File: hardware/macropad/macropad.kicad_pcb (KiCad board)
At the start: 2 copper layers, 6.5 x 0.7 mm, 84 parts, among them J1 SWD, J2 USB_C_Receptacle, J3 Conn_01x04_Pin, J4 display(4x1), J5 USB_A, J6 Enc2, J6 enc2, J7 Conn_01x04_Pin, J7 Enc1, J8 USB_A, J9 Conn_02x03_Counter_Clockwise, Q1 Q_PMOS, Q2 FS8205A, SW1 SW_Push, SW10 SW_SPDT, SW11 SW_Push, SW12 Enc1, SW12 SW_Push, SW2 SW_Push, SW3 SW_Push, SW4 SW_Push, SW5 SW_Push, SW6 SW_Push, SW7 SW_Push, SW8 SW_Push, SW9 SW_Push, U1 AP2112K-3.3, U1 LP2992IM5-3.3/NOPB, U2 STM32F103C8Tx, U3 NRF24L01_Breakout, U4 STM32F103C8Tx, U5 NRF24L01_Breakout, U6 TP4056-42-ESOP8, U7 DW01A, U8 RT8010AGQW, Y1 8Mhz C_L=12pF, Y2 8Mhz

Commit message: added usba fp, updated pcb, 5v to vbus
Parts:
- removed C32: 0.1u, Capacitor_SMD:C_0603_1608Metric
- removed C33, C35: 10u, Capacitor_SMD:C_0805_2012Metric
- removed C34: 4.7u, Capacitor_SMD:C_0603_1608Metric
- removed J2: USB_C_Receptacle, usbc:TYPE-C-SMD_U263-163N-4GS1735
- removed the J6 at (85.9, 37.6)
- removed the J6 at (247.3, 72.9)
- removed the J7 at (42.6, 54.4)
- removed the J7 at (251.9, 72.9)
- removed J9: Conn_02x03_Counter_Clockwise, Connector_PinHeader_2.54mm:PinHeader_2x03_P2.54mm_Vertical
- removed Q1: Q_PMOS, Package_TO_SOT_SMD:SOT-23-3
- removed the R11 at (256.4, 72.1)
- removed the R11 at (34.3, 69.7)
- removed the R12 at (34.3, 72.7)
- removed the R12 at (256.4, 75.0)
- removed the SW12 at (74.9, 114.3)
- removed the SW12 at (26.8, 71.1)
- removed the U1 at (162.6, 130.5)
- removed the U1 at (268.1, 73.2)
- added C16: 10n, Capacitor_SMD:C_0603_1608Metric, F.Cu at (53.4, 163.9)
- added C24: 0.1u, Capacitor_SMD:C_0603_1608Metric, F.Cu at (75.8, 88.3)
- added C25: 0.1u, Capacitor_SMD:C_0603_1608Metric, F.Cu at (75.8, 90.8)
- added C26: 10u, Capacitor_SMD:C_0805_2012Metric, F.Cu at (76.0, 105.7)
- added C27: 4.7u, Capacitor_SMD:C_0603_1608Metric, F.Cu at (75.8, 93.3)
- added C28: 1u, Capacitor_SMD:C_0805_2012Metric, F.Cu at (76.0, 108.7)
- added C29: 10n, Capacitor_SMD:C_0603_1608Metric, F.Cu at (75.8, 95.9)
- added C30: 2.2u, Capacitor_SMD:C_0603_1608Metric, F.Cu at (75.8, 98.4)
- added J6: Enc2, Connector_PinHeader_2.54mm:PinHeader_1x05_P2.54mm_Vertical, F.Cu at (187.7, 97.8)
- added J7: Enc1, Connector_PinHeader_2.54mm:PinHeader_1x05_P2.54mm_Vertical, F.Cu at (187.7, 119.4)
- added R11: 10k, Resistor_SMD:R_0805_2012Metric, F.Cu at (89.3, 47.0)
- added R12: 10k, Resistor_SMD:R_0805_2012Metric, F.Cu at (112.6, 38.9)
- added SW12: SW_SPDT, Button_Switch_THT:SW_Slide_SPDT_Angled_CK_OS102011MA1Q, F.Cu at (65.5, 90.3)
- added SW13: SW_SPDT, Button_Switch_THT:SW_Slide_SPDT_Angled_CK_OS102011MA1Q, F.Cu at (65.5, 100.7)
- added U1: LP2992IM5-3.3/NOPB, LP2992:DBV0005A_N, F.Cu at (55.1, 180.6)
- added U9: LP2992IM5-3.3/NOPB, LP2992:DBV0005A_N, F.Cu at (63.9, 110.3)
- C21: footprint Capacitor_SMD:C_0805_2012Metric -> Capacitor_SMD:C_0603_1608Metric
- C31: value 0.1u -> 10u; footprint Capacitor_SMD:C_0603_1608Metric -> Capacitor_SMD:C_0805_2012Metric
- J3: moved to B.Cu
- J5: footprint Connector_PinHeader_2.54mm:PinHeader_1x05_P2.54mm_Horizontal -> usbA:U-G-O4DD-W-1
- J8: value USB_A -> Conn_01x02; footprint Connector_USB:USB_A_Connfly_DS1095 -> Connector_Wire:SolderWire-0.5sqmm_1x02_P4.6mm_D0.9mm_OD2.1mm
- R10: value 100 -> 1.2k
- R13: value 10k -> 1k; footprint Resistor_SMD:R_0805_2012Metric -> Resistor_SMD:R_0603_1608Metric
- R14: value 1.5K -> 100
- R6: value 1k -> 1.5K
- R7: value 1k -> 10k; footprint Resistor_SMD:R_0603_1608Metric -> Resistor_SMD:R_0805_2012Metric
- R8: value 1.2k -> 1k
- SW10: value SW_SPDT -> SW_Push; footprint keyswitches:Kailh_socket_MX -> Button_Switch_SMD:SW_Push_1P1T_NO_E-Switch_TL3301NxxxxxG; moved to B.Cu
- U8: footprint RT8010:WQFN16_RT8010_RIT-M -> RT8010:WQFN16_RT8010_RIT
- moved R3 244.8 mm to (41.2, 175.9)
- moved R13 184.3 mm to (79.8, 95.9)
- moved Q2 176.3 mm to (78.9, 101.9)
- moved D2 173.7 mm to (82.3, 113.1)
- moved U8 173.4 mm to (89.3, 112.9)
- moved U5 117.6 mm to (69.1, 158.1), turned to 90 degrees
- moved C13 113.3 mm to (36.7, 178.9)
- moved U4 109.7 mm to (74.5, 167.2), turned to -90 degrees
- moved SW10 100.4 mm to (74.2, 143.7), turned to 180 degrees
- moved C14 93.3 mm to (53.4, 158.9)
- moved C15 92.8 mm to (53.4, 161.4)
- moved U6 90.6 mm to (82.4, 107.6)
- moved J5 89.5 mm to (74.5, 177.8)
- moved Y1 87.3 mm to (142.7, 67.2)
- moved C21 85.2 mm to (57.4, 156.4)
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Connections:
- net /Power/out+ renamed out+
- C17 pad 2: GND_DGL -> GND
- C18 pad 2: GND_DGL -> GND
- C31 pad 1: +5V -> /Power/Vout_buck
- D1 pad 2: +5V -> VBUS
- D2 pad 2: +5V -> VBUS
- D3 pad 2: +5V -> VBUS
- J8 pad 1: VBUS -> /Power/B+
- J8 pad 2: /dongle/USB_D- -> /Power/B-
- L1 pad 2: /Power/Vout -> /Power/Vout_buck
- Q2 pad 6: GND -> /Power/out-
- Q2 pad 7: GND -> /Power/out-
- R10 pad 1: Net-(U7-VCC) -> Net-(U6-PROG)
- R10 pad 2: /Power/B+ -> GND
- R13 pad 1: /dongle/BOOT0_DGL -> Net-(U7-CS)
- R13 pad 2: GND_DGL -> /Power/out-
- R14 pad 1: +3.3V_DGL -> Net-(U7-VCC)
- R14 pad 2: /dongle/USB_D+_DGL -> /Power/B+
- R5 pad 1: +5V -> /dongle/BOOT0_DGL
- R5 pad 2: GND -> GND_DGL
- R6 pad 1: Net-(U6-~{CHRG}) -> +3.3V_DGL
- R6 pad 2: Net-(D1-K) -> /dongle/USB_D+_DGL
- R7 pad 1: Net-(U6-~{STDBY}) -> VBUS
- R7 pad 2: Net-(D3-K) -> GND
- R8 pad 1: Net-(U6-PROG) -> Net-(U6-~{CHRG})
- R8 pad 2: GND -> Net-(D1-K)
- R9 pad 1: Net-(U7-CS) -> Net-(U6-~{STDBY})
- R9 pad 2: GND -> Net-(D3-K)
- SW10 pad 1: /BAT_OUT_ON -> /dongle/NRST_DGL
- SW10 pad 2: /BAT_OUT -> GND_DGL
- U6 pad 4: +5V -> VBUS
- U6 pad 8: +5V -> VBUS
- U8 pad 4: /Power/Vout -> /Power/Vout_buck
- Y1 pad 2: GND_DGL -> GND
- Y1 pad 4: GND_DGL -> GND
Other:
- board outline removed

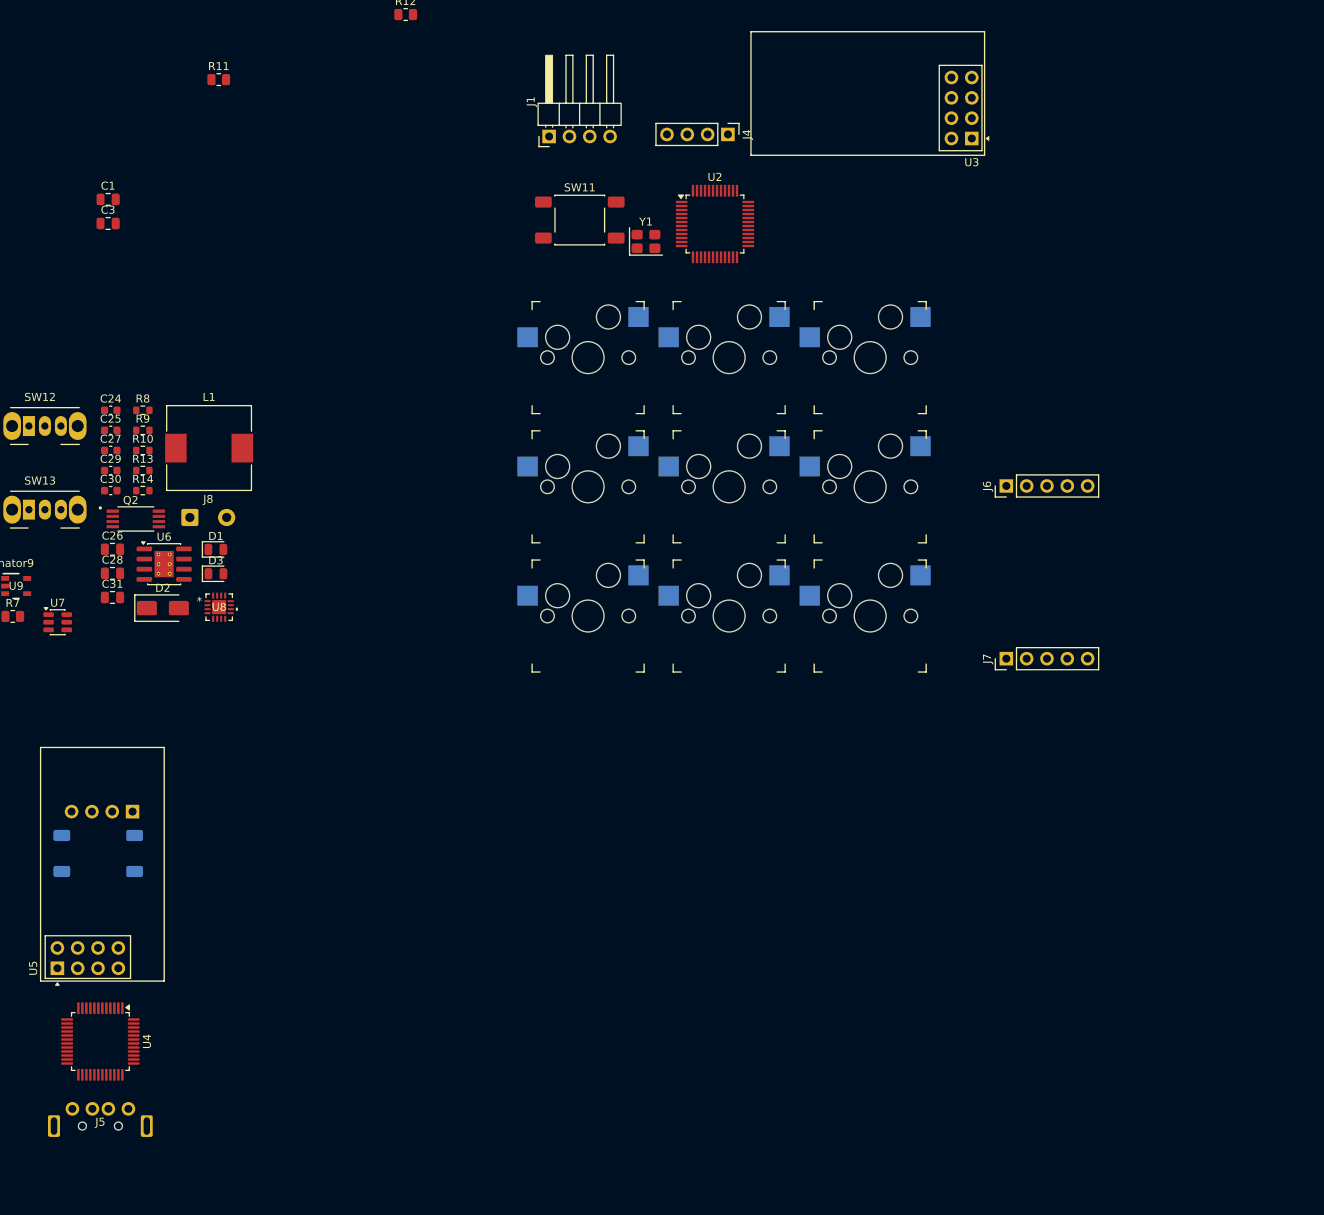
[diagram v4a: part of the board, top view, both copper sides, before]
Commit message: replaced buttons with pads
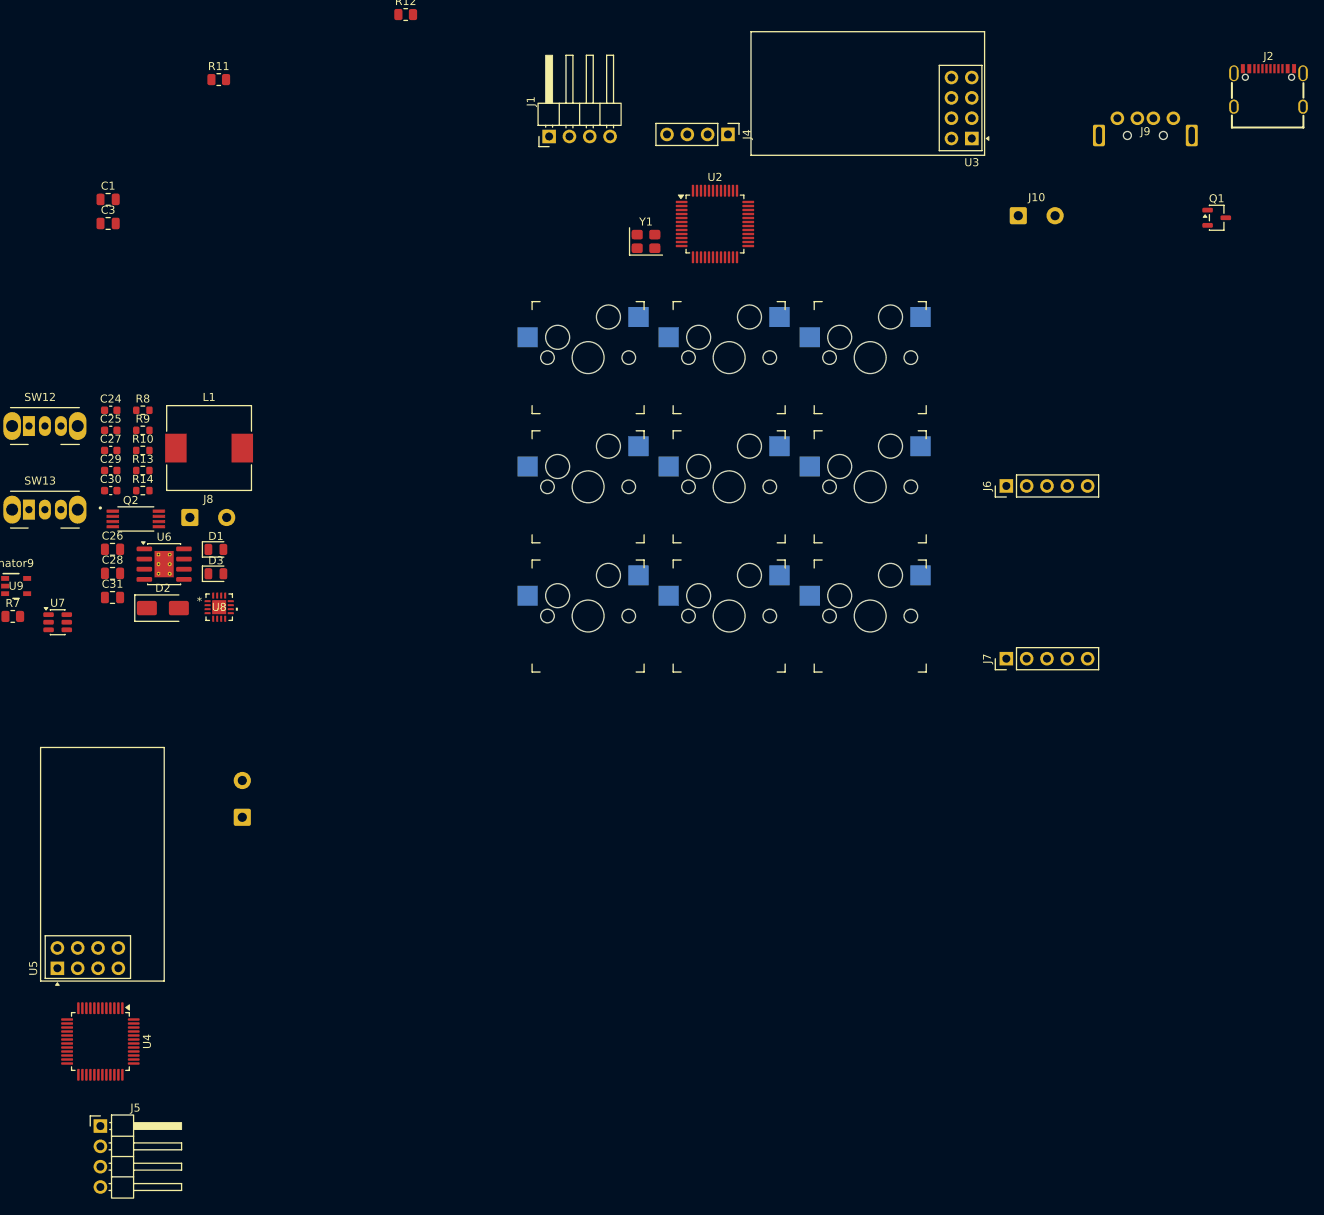
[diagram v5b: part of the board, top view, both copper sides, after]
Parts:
- removed SW10, SW11: SW_Push, Button_Switch_SMD:SW_Push_1P1T_NO_E-Switch_TL3301NxxxxxG
- added J10: Conn_01x02, Connector_Wire:SolderWire-0.5sqmm_1x02_P4.6mm_D0.9mm_OD2.1mm, F.Cu at (189.2, 64.0)
- added J2: USB_C_Receptacle, usbc:TYPE-C-SMD_U263-163N-4GS1735, F.Cu at (220.5, 48.0)
- added J9: USB_A, usbA:U-G-O4DD-W-1, F.Cu at (205.1, 54.0)
- added Q1: Q_PMOS, Package_TO_SOT_SMD:SOT-23-3, F.Cu at (214.0, 64.3)
- J3: value Conn_01x04_Pin -> Conn_01x02; footprint Connector_PinHeader_2.54mm:PinHeader_1x04_P2.54mm_Horizontal -> Connector_Wire:SolderWire-0.5sqmm_1x02_P4.6mm_D0.9mm_OD2.1mm
- J5: value USB_A -> Conn_01x04_Pin; footprint usbA:U-G-O4DD-W-1 -> Connector_PinHeader_2.54mm:PinHeader_1x04_P2.54mm_Horizontal
- moved J3 13.7 mm to (92.2, 139.2)
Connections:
- J3 pad 1: +3.3V_DGL -> /NRST
- J3 pad 2: /dongle/SWDIO_DGL -> GND
- J5 pad 1: VBUS_DGL -> +3.3V_DGL
- J5 pad 2: /dongle/USB_D-_DGL -> /dongle/SWDIO_DGL
- J5 pad 3: /dongle/USB_D+_DGL -> /dongle/SWCLK_DGL
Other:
- board outline added: 6.5 x 0.7 mm

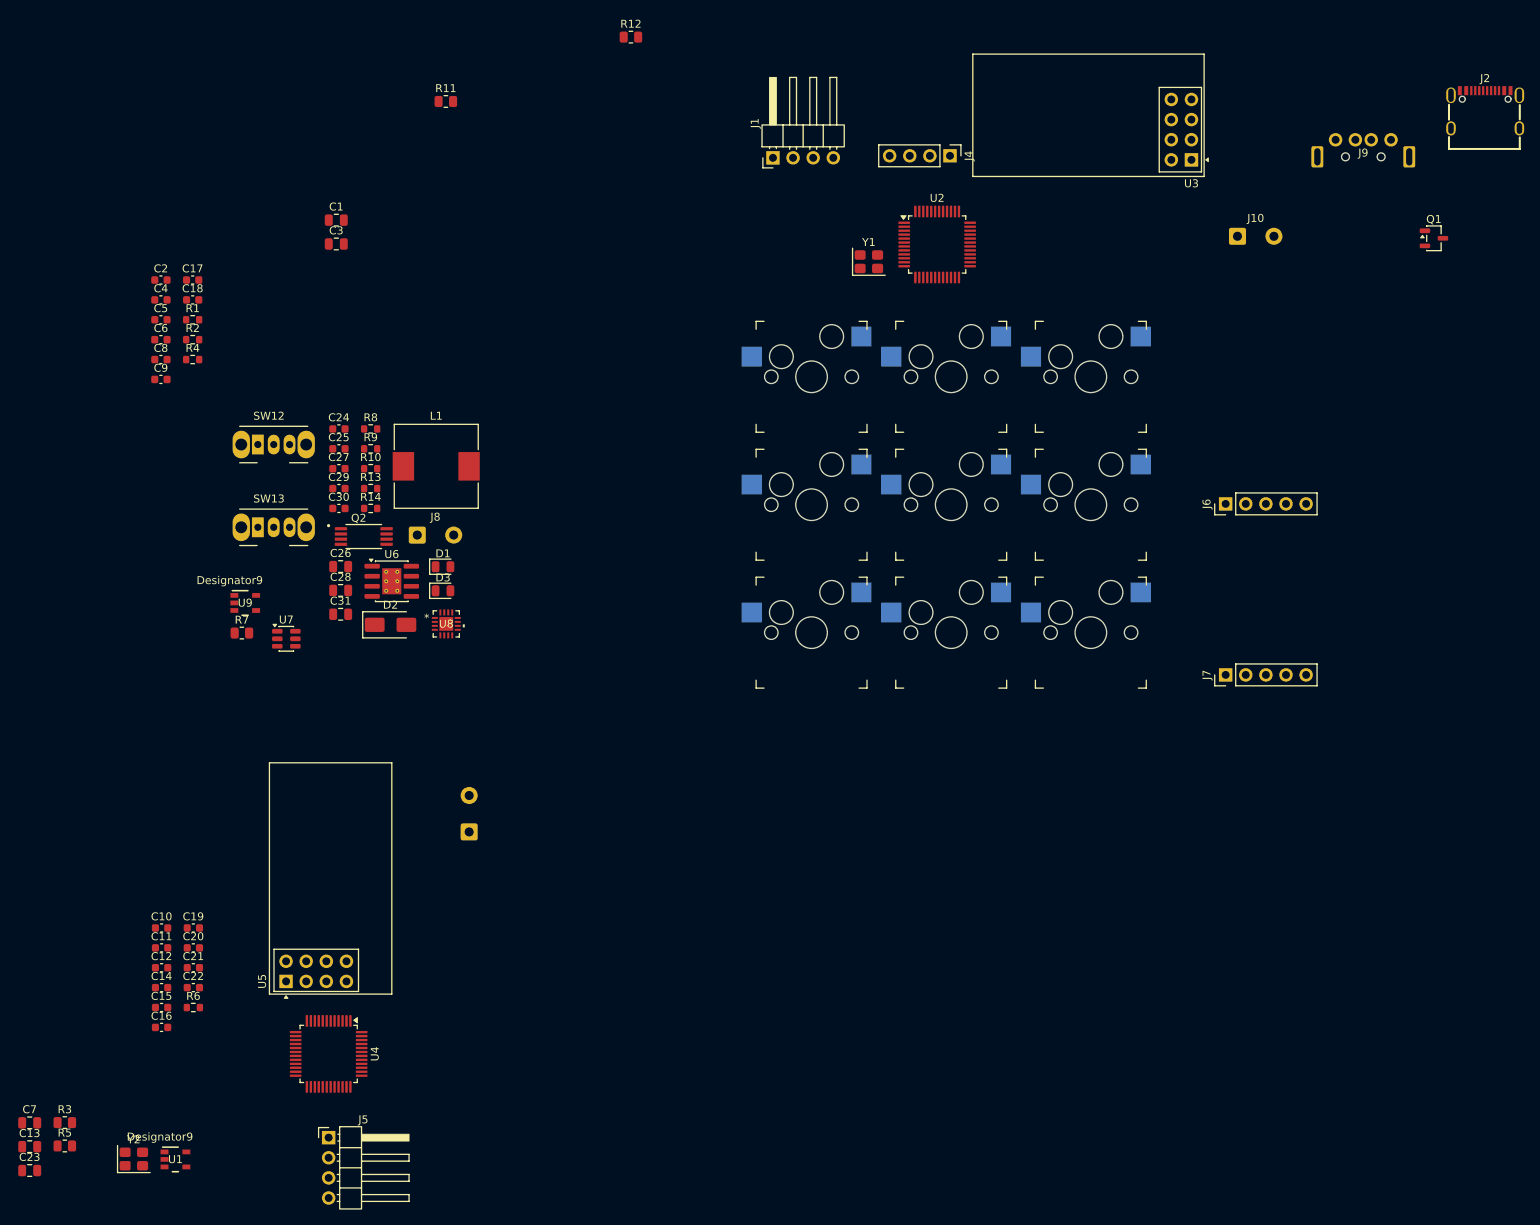
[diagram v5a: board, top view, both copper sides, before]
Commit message: updated usb-c receptacle footprint
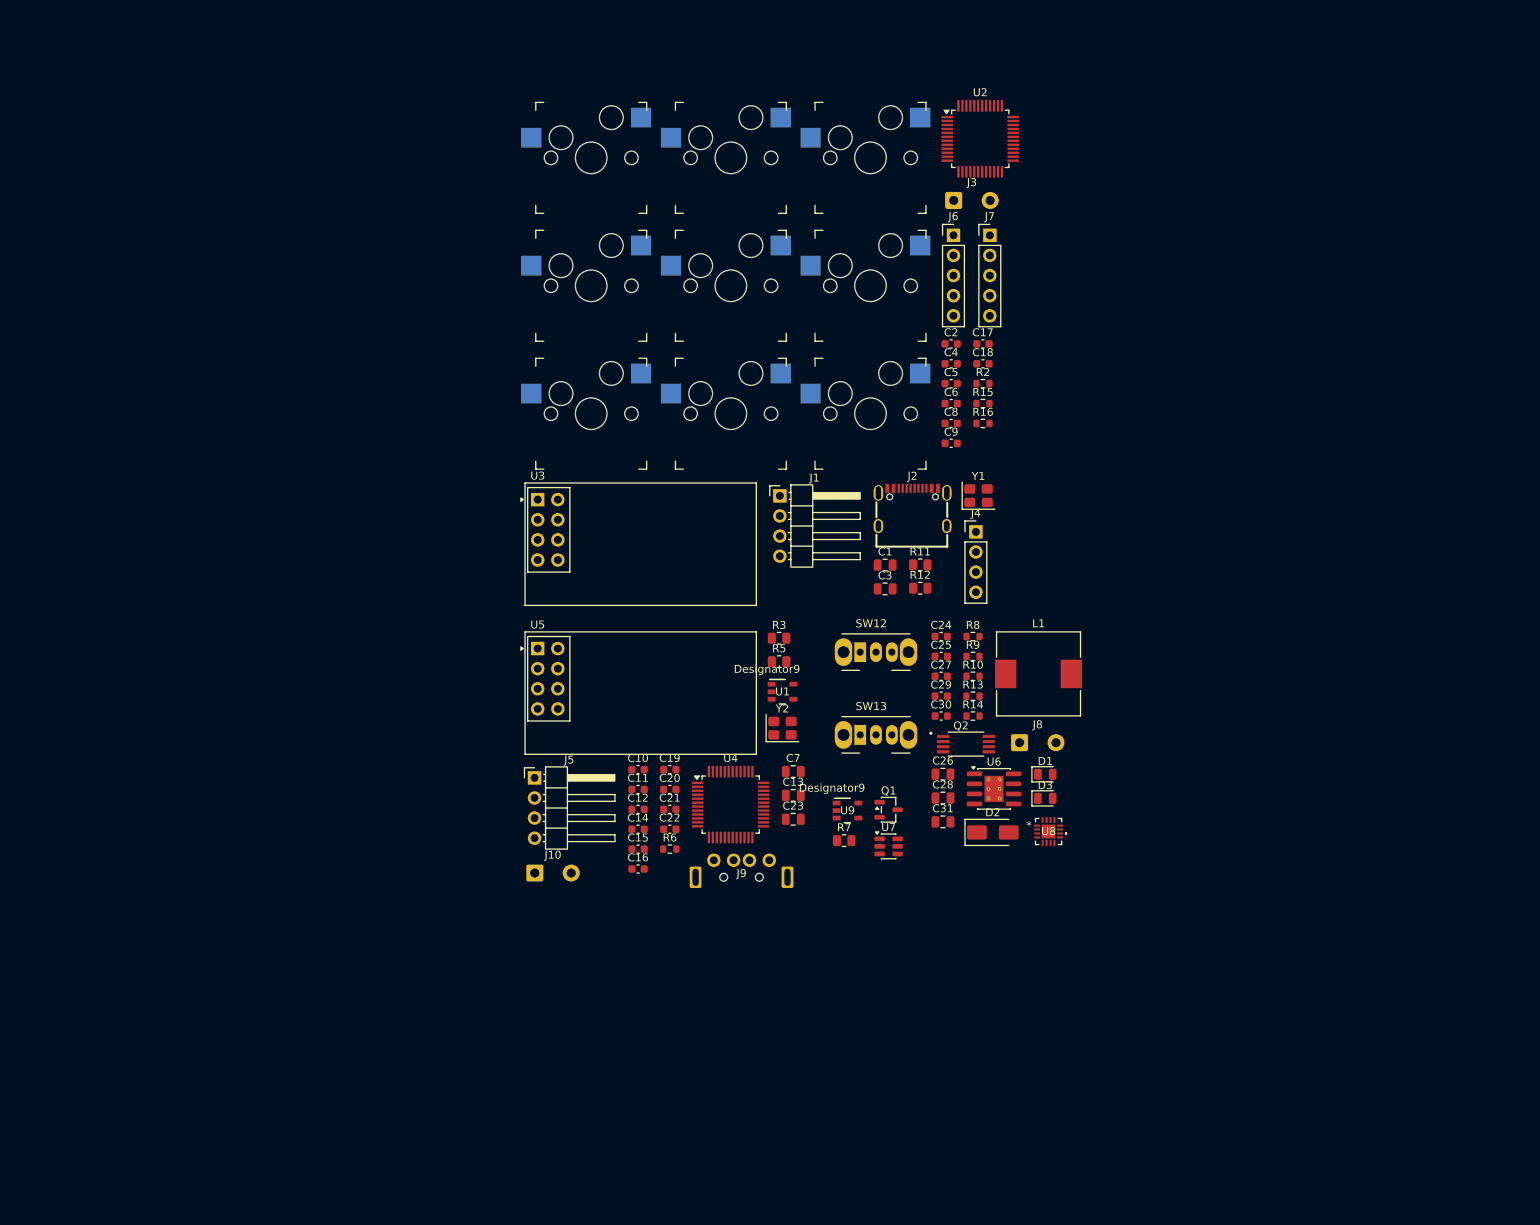
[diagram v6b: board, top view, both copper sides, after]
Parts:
- removed R1, R4: 5.1k, Resistor_SMD:R_0603_1608Metric
- added R15: 5.1k, Resistor_SMD:R_0603_1608Metric, F.Cu at (157.1, 85.1)
- added R16: 5.1k, Resistor_SMD:R_0603_1608Metric, F.Cu at (157.1, 87.6)
- J2: value USB_C_Receptacle -> USB_C_Receptacle_USB2.0_16P
- J3: moved to F.Cu
- moved J9 120.1 mm to (126.6, 144.9)
- moved J10 119.7 mm to (100.5, 144.4)
- moved R3 109.0 mm to (131.3, 114.8)
- moved R5 109.0 mm to (131.3, 117.7)
- moved C13 106.1 mm to (133.1, 134.6)
- moved C23 106.1 mm to (133.1, 137.6)
- moved C7 106.1 mm to (133.1, 131.6)
- moved J3 100.5 mm to (153.4, 59.5), turned to 0 degrees
- moved C2 100.1 mm to (153.1, 77.6)
- moved C4 100.1 mm to (153.1, 80.1)
- moved C5 100.1 mm to (153.1, 82.6)
- moved C6 100.1 mm to (153.1, 85.1)
- moved C8 100.1 mm to (153.1, 87.6)
- moved C9 100.1 mm to (153.1, 90.1)
- moved C17 100.1 mm to (157.1, 77.6)
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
